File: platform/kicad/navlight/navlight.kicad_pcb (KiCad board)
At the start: 2 copper layers, 36.5 x 40 mm, 8 parts, among them J1 TSL2951, J2 Conn_01x05_Pin

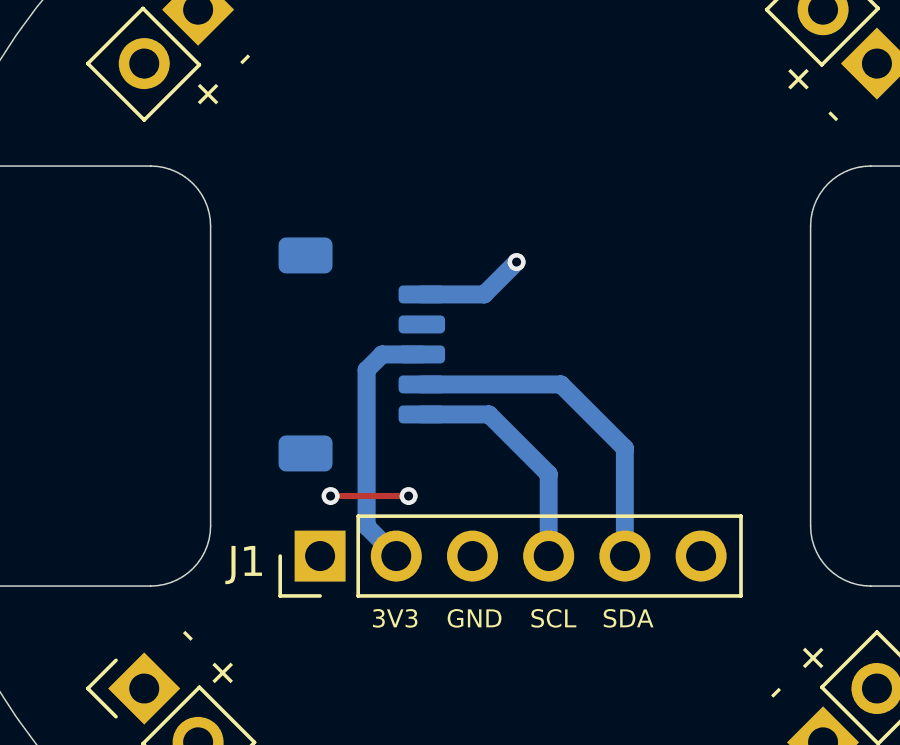
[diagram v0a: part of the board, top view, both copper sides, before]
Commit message: Navlight: Update port position
This change reverts the position of the JST to the same side of the
PCB as the lightsensor.

This change also adds the production files to the repo.
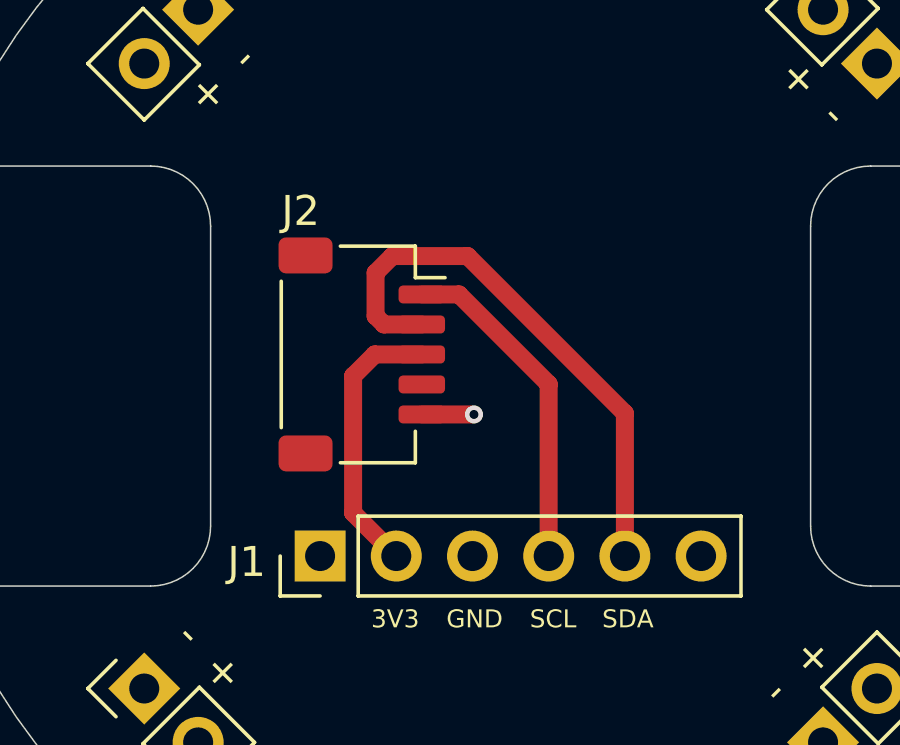
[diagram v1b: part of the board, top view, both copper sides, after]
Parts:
- J2: moved to F.Cu
- turned J2 to -90 degrees
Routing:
- net SDA: track 11.2 -> 18.6 mm
- net SCL: track 7.78 -> 11.2 mm
- net GND: track 2.80 -> 0.00 mm, vias 2 -> 0
- net NAV: track 3.61 -> 1.74 mm
- net +3V3: track 8.67 -> 9.18 mm
- added copper zone on F.Cu, net GND
- added copper zone on B.Cu, net NAV
- removed copper zone on B.Cu, net GND
- removed copper zone on F.Cu, net NAV
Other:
- board text added: "Navlight PCB v1revB Designed By David Sutton <david@ausocean.org>"
- board text removed: "Navlight PCB v0.1 Designed By David Sutton <david@ausocean.org>"
